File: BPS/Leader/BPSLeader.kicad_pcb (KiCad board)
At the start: 2 copper layers, 100 x 75 mm, 154 parts, among them J1 GPIO Analyzer, J10 CAN_Out, J11 ErrorLightConn, J12 USB_B_Micro, J13 FanBrdConn, J2 Volt/Temp SPI Analyzer, J3 Current SPI Analyzer, J4 CAN Analyzer, J5 SWD, J6 PowerConn, J7 MinionConn, J8 CurrentConn, J9 ContactorConn, Q1 NTR4003NT1G, Q2 VND5N07-E, Q3 NTR4003NT1G, Q4 VND5N07-E, SW1 B3SL-1002P, U1 STM32F413RHTx, U10 ADM3055E, U11 CDSOT23-T24CAN, U12 SI8261ABC-IS, U13 CP2102N-A01-GQFN24, U14 SI8261ABC-IS, U15 SI8261ABC-IS, U16 SI8261ABC-IS, U17 SI8261ABC-IS, U18 MCP112, U19 RN4871-I, U2 RI3-1205S, U3 NCP1117-3.3_SOT223, U4 M24128, U5 LTC6820, U6 LTC6820, U7 HX1188FNL, U8 SI8261ABC-IS, U9 BAS70-04, Y1 8M

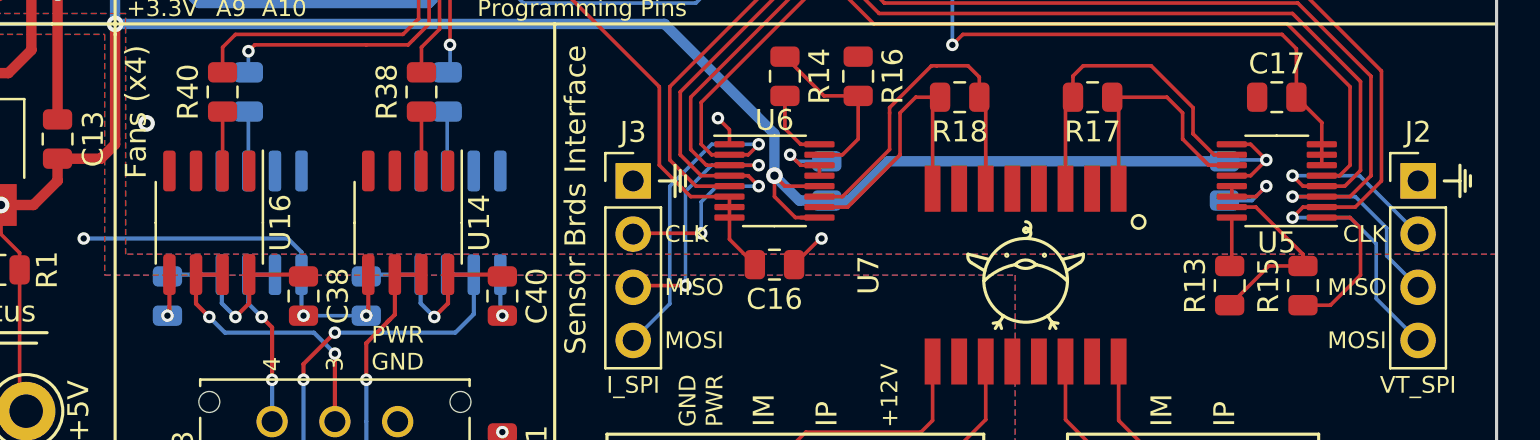
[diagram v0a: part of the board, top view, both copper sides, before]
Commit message: Adds copper cutout to transformer for isospi because ltc6820 datasheet recommended it
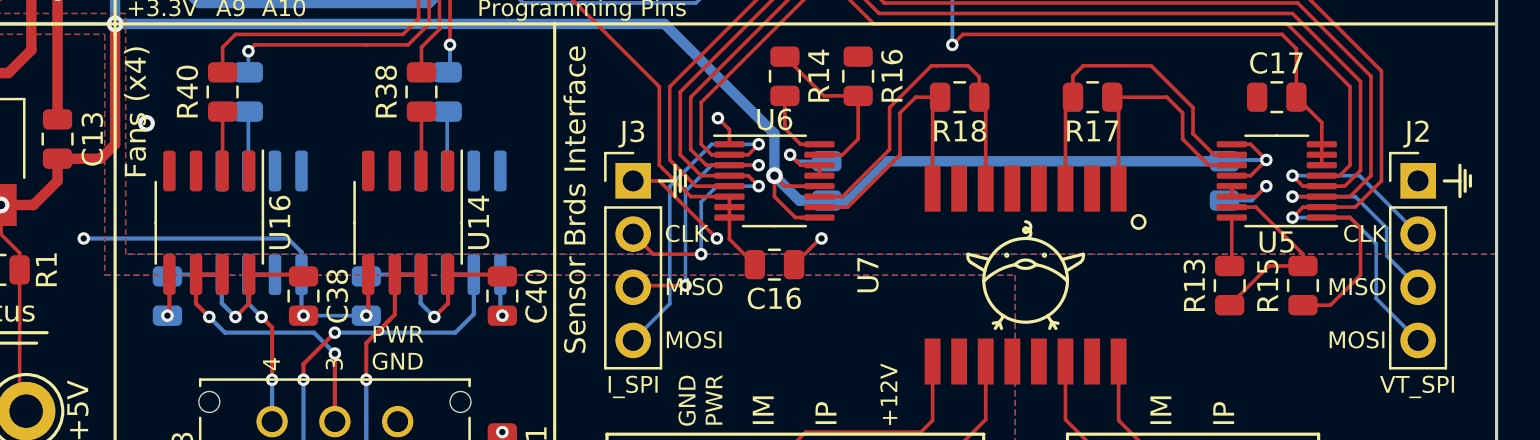
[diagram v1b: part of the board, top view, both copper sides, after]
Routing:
- net GND: track 192.9 -> 198.0 mm, vias 23 -> 24
- net /SPI3_CLK: track 24.7 -> 26.1 mm

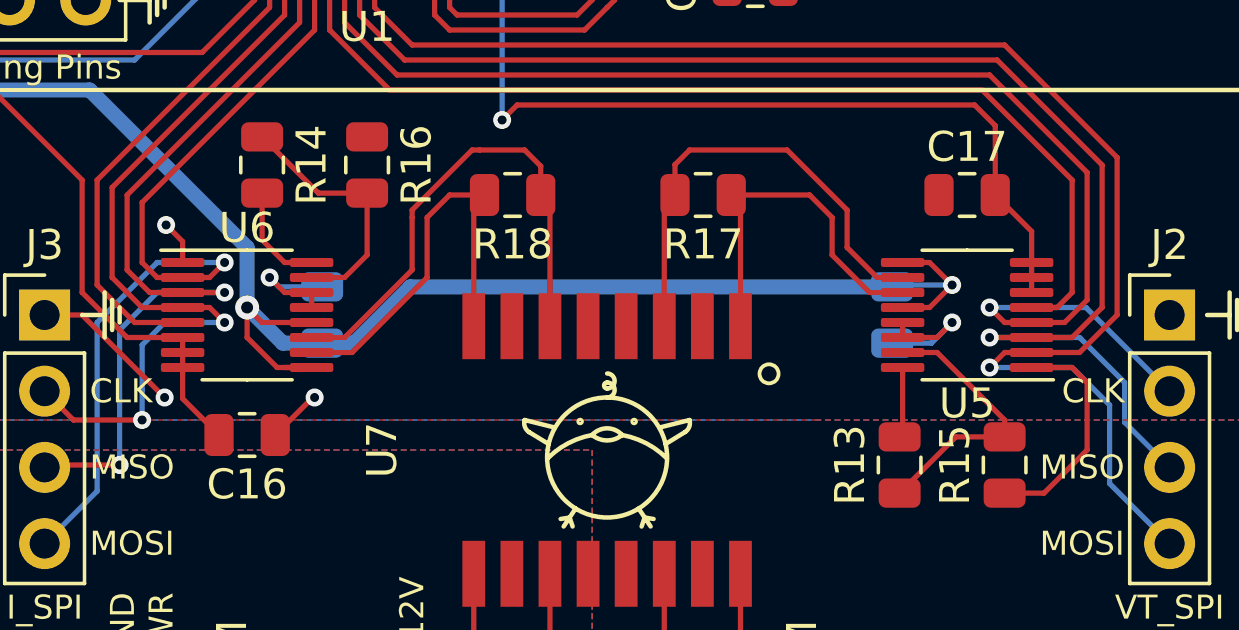
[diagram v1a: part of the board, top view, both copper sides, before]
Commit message: Changes LTC6820 POL and PHA pins to +5V due to VIH and VIL parameters in datasheet
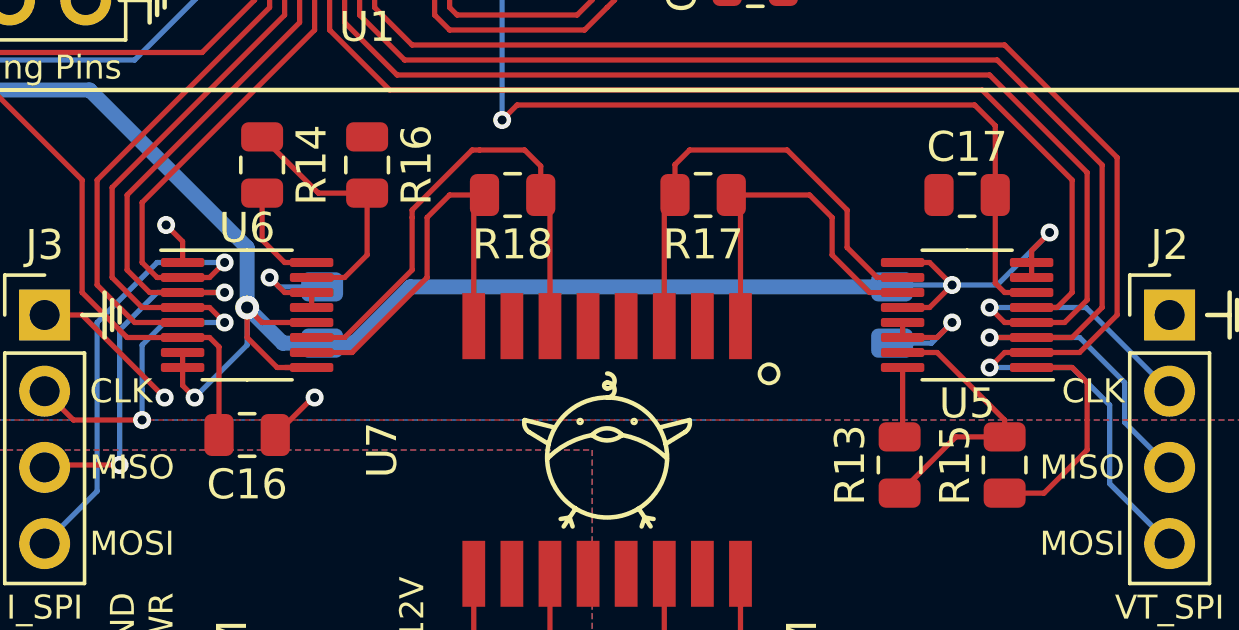
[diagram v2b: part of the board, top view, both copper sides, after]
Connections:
- U5 pad 7: +3V3 -> +5V
- U5 pad 8: +3V3 -> +5V
- U6 pad 7: +3V3 -> +5V
- U6 pad 8: +3V3 -> +5V
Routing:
- net +5V: track 225.1 -> 236.2 mm, vias 12 -> 14
- net +3V3: track 318.5 -> 319.6 mm
